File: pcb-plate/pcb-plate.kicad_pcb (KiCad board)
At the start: 2 copper layers, 135.3 x 96.4 mm, 24 parts, among them SW1 SW_Push, SW10 SW_Push, SW11 SW_Push, SW12 SW_Push, SW13 SW_Push, SW14 SW_Push, SW15 SW_Push, SW16 SW_Push, SW17 SW_Push, SW18 SW_Push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

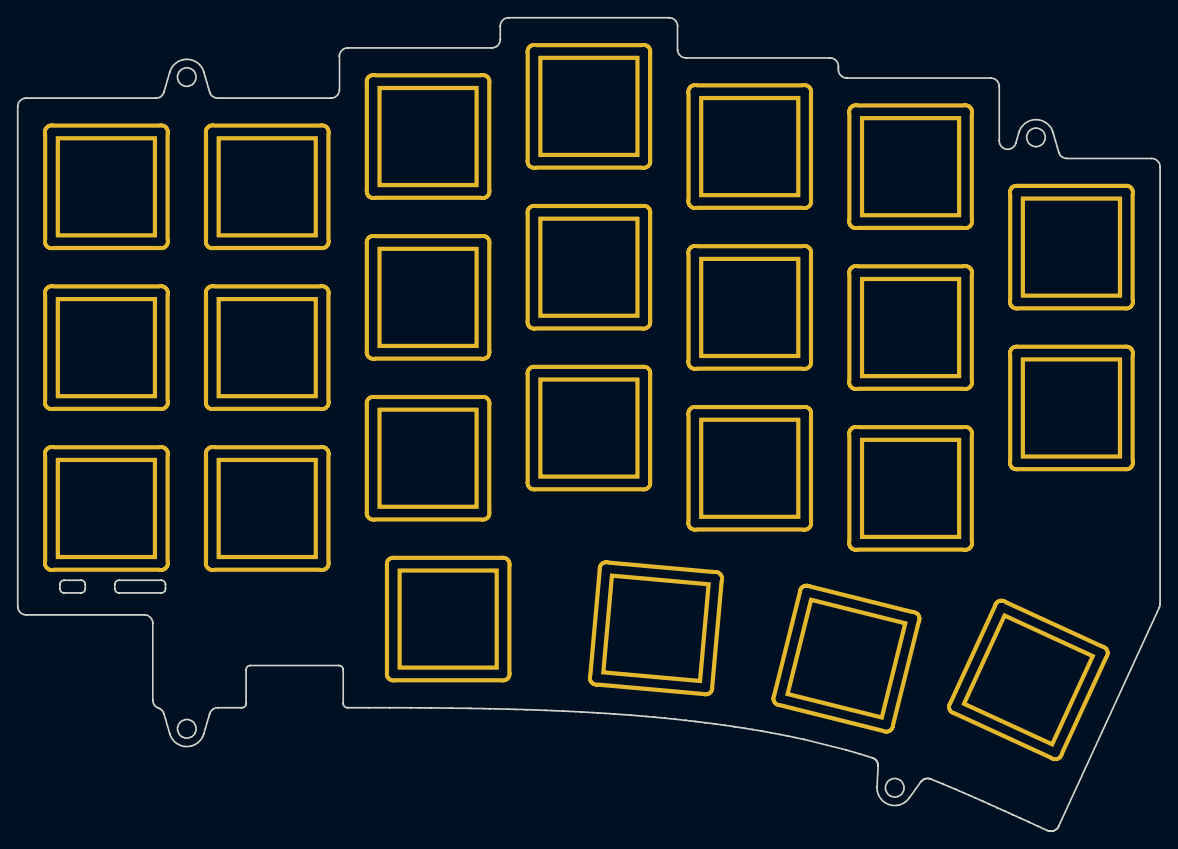
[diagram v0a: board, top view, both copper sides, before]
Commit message: Update PCB plate
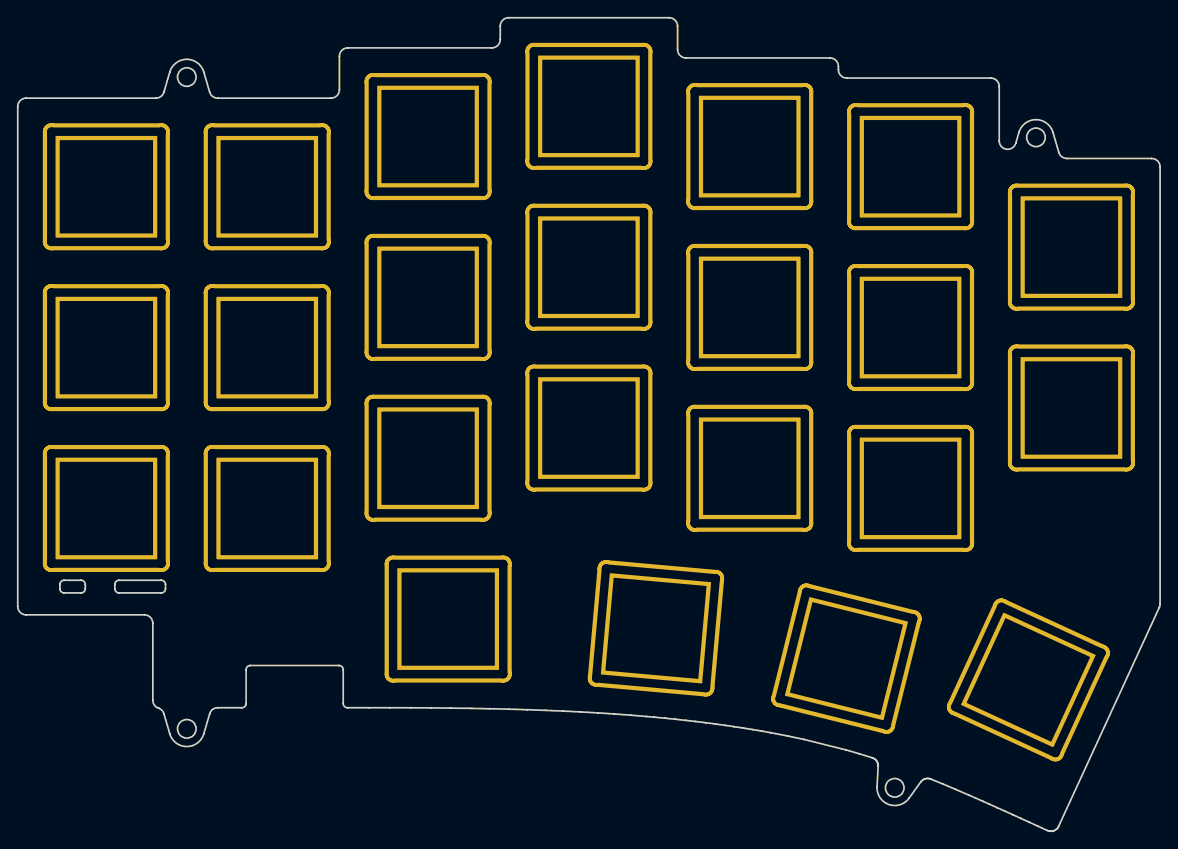
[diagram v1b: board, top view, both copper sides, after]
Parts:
- added H1: MountingHole, locallib:logo1, F.Cu at (82.8, 117.5)
